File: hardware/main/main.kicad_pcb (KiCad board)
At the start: 2 copper layers, 83.3 x 74.9 mm, 52 parts, among them P1 CONN_01X08, P2 CONN_01X08, P3 CONN_01X16, U1 TSL235, U10 TSL235, U11 TSL235, U12 TSL235, U13 TSL235, U14 TSL235, U15 TSL235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

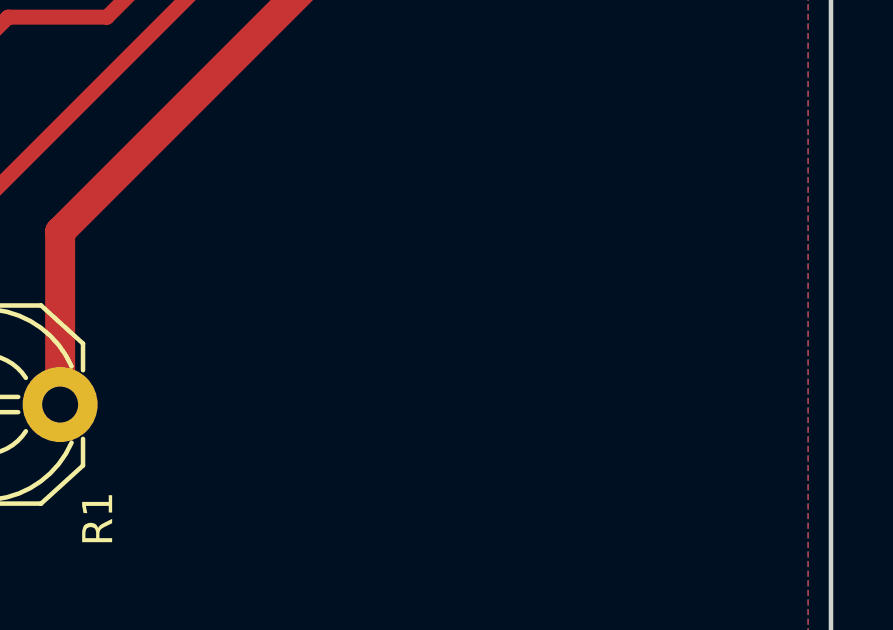
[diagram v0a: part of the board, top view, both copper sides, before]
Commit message: added text to Front layer
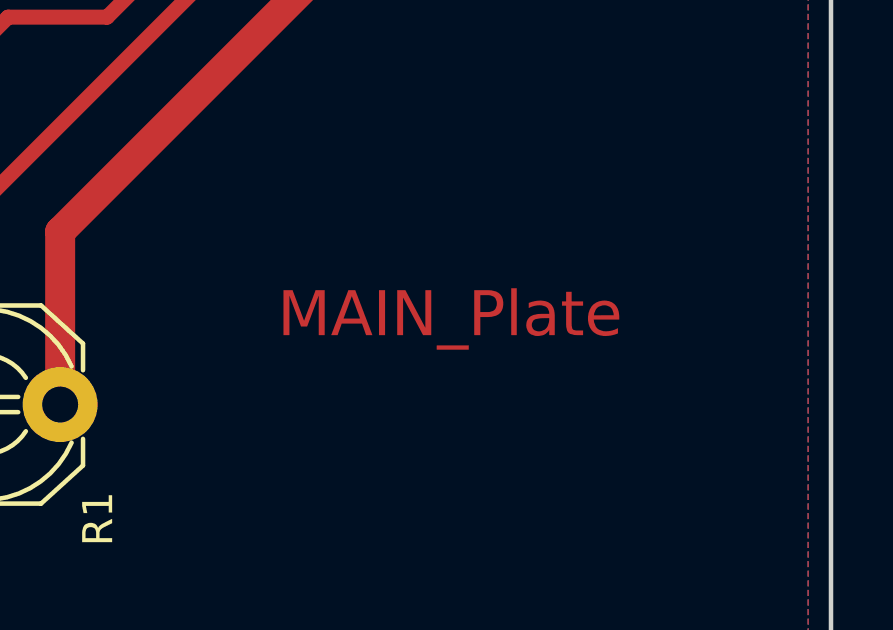
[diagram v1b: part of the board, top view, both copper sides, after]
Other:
- board text added: "MAIN_Plate"
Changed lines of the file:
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@@
-(kicad_pcb (version 4) (host pcbnew 4.0.5-e0-6337~52~ubuntu16.10.1)
+(kicad_pcb (version 4) (host pcbnew 4.0.6-e0-6349~52~ubuntu16.10.1)
   (general
     (links 112)
-    (no_connects 0)
+    (no_connects 51)
     (area 31.928999 48.438999 115.391001 123.519001)
     (thickness 1.6)
-    (drawings 18)
+    (drawings 19)
     (tracks 270)
     (zones 0)
@@
     (pad 1 thru_hole circle (at 0 0) (size 1.524 1.524) (drill 0.762) (layers *.Cu)
       (net 6 GND) (zone_connect 2))
+  )
+  (gr_text MAIN_Plate (at 102.616 110.49) (layer F.Cu)
+    (effects (font (size 1.5 1.5) (thickness 0.3)))
   )
   (gr_line (start 32.004 123.444) (end 38.1 123.444) (angle 90) (layer Edge.Cuts) (width 0.15))
@@
     (connect_pads (clearance 0.508))
     (min_thickness 0.254)
-    (fill yes (arc_segments 16) (thermal_gap 0.508) (thermal_bridge_width 0.508))
+    (fill (arc_segments 16) (thermal_gap 0.508) (thermal_bridge_width 0.508))
     (polygon
       (pts
@@
     (connect_pads (clearance 0.508))
     (min_thickness 0.254)
-    (fill yes (arc_segments 16) (thermal_gap 0.508) (thermal_bridge_width 0.508))
+    (fill (arc_segments 16) (thermal_gap 0.508) (thermal_bridge_width 0.508))
     (polygon
       (pts
